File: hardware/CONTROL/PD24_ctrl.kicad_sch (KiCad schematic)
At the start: 7 parts, among them J1 Conn_01x12_Socket, J2 Conn_01x08_Socket, SW1 SW_Push, SW2 SW_Push, SW3 SW_Push, U1 STM32G031G8Ux, U2 ips_0.96_16080

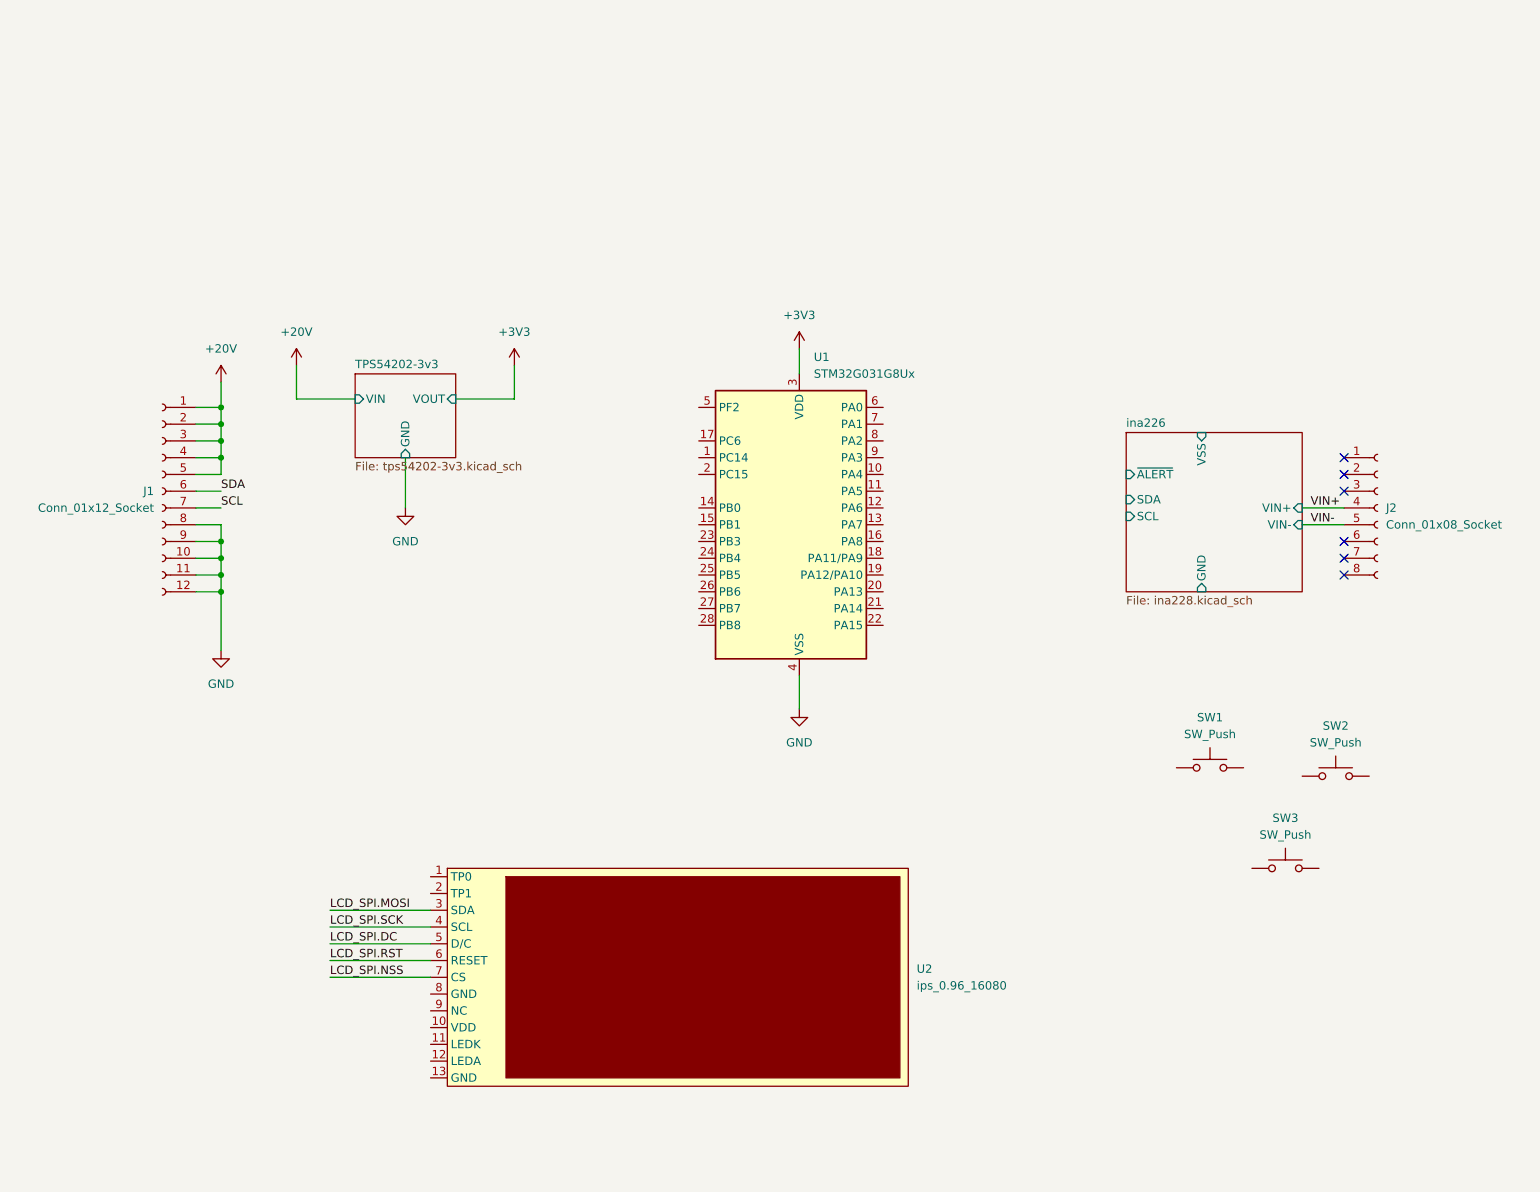
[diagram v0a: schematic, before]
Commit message: PD24 控制部分的PCB设计完成
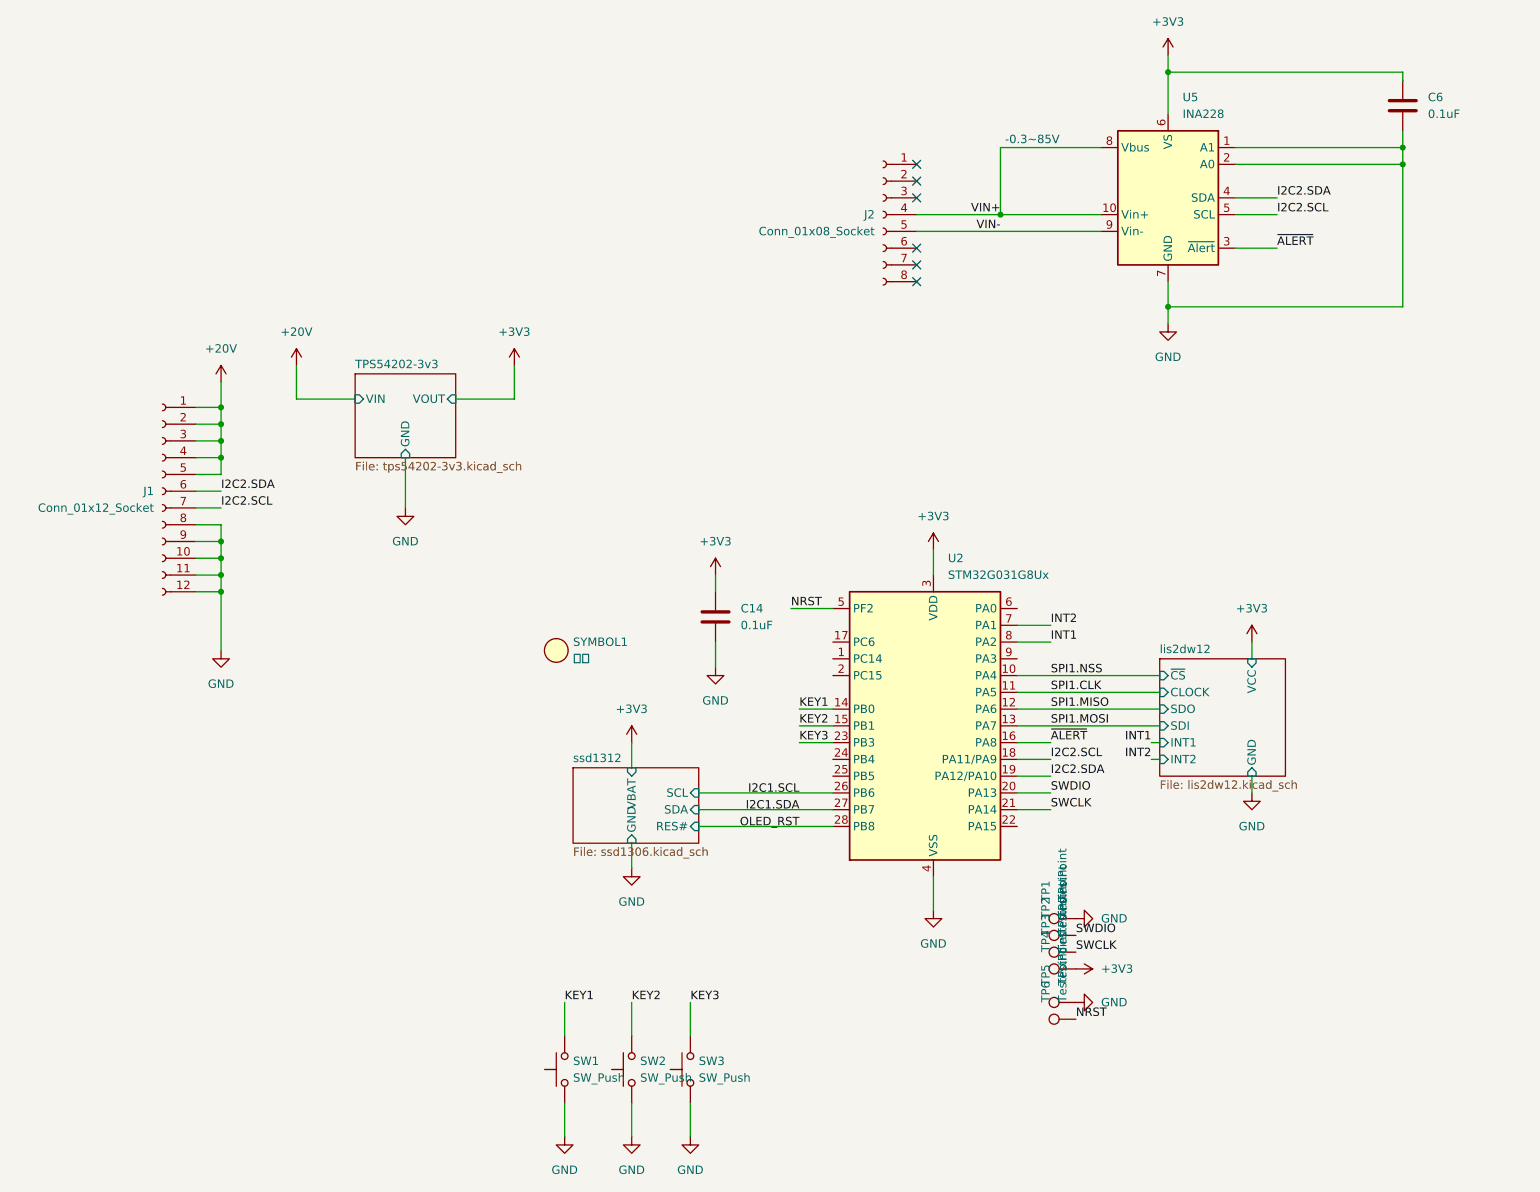
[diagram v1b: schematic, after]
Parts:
- removed U2: ips_0.96_16080, my_footprint:ips-16080-0.96, symbol my_symbol:ips_0.96_16080
- added C14, C6: 0.1uF, Capacitor_SMD:C_0603_1608Metric, symbol Device:C
- added SYMBOL1: 符号, Symbol:KiCad-Logo2_5mm_Copper, symbol my_symbol:symbol
- added TP1, TP2, TP3, TP4, TP5, TP6: TestPoint, TestPoint:TestPoint_Pad_D1.0mm, symbol Connector:TestPoint
- added U5: INA228, Package_SO:VSSOP-10_3x3mm_P0.5mm, symbol Sensor_Energy:INA228
- renumbered U1 to U2
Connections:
- net SCL is gone; now on net I2C2.SCL: J1.7 (Pin_7)
- net SDA is gone; now on net I2C2.SDA: J1.6 (Pin_6)
- net +3V3: now also C14.1, C6.1, TP4.1, U5.6 (VS)
- net GND: now also SW1.1, SW2.1, SW3.1, C14.2, C6.2, TP1.1, TP5.1, U5.1 (A1), U5.2 (A0), U5.7 (GND)
- net VIN+: now also U5.10 (Vin+), U5.8 (Vbus)
- net VIN-: now also U5.9 (Vin-)
- net SPI1.NSS: now reaches U2.10 (PA4)
- net SPI1.CLK: now reaches U2.11 (PA5)
- net SPI1.MISO: now reaches U2.12 (PA6)
- net SPI1.MOSI: now reaches U2.13 (PA7)
- net KEY1: now reaches U2.14 (PB0)
- net KEY1: now also SW1.2
- net KEY2: now reaches U2.15 (PB1)
- net KEY2: now also SW2.2
- net ~{ALERT}: now reaches U2.16 (PA8)
- net ~{ALERT}: now also U5.3 (~{Alert})
- net I2C2.SCL: now reaches U2.18 (PA11/PA9)
- net I2C2.SCL: now also U5.5 (SCL)
- net I2C2.SDA: now reaches U2.19 (PA12/PA10)
- net I2C2.SDA: now also U5.4 (SDA)
- net SWDIO: now reaches U2.20 (PA13)
- net SWDIO: now also TP2.1
- net SWCLK: now reaches U2.21 (PA14)
- net SWCLK: now also TP3.1
- net KEY3: now reaches U2.23 (PB3)
- net KEY3: now also SW3.2
- net ssd1312/SCL: now reaches U2.26 (PB6)
- net ssd1312/SDA: now reaches U2.27 (PB7)
- net ssd1312/RES#: now reaches U2.28 (PB8)
- net NRST: now reaches U2.5 (PF2)
- net NRST: now also TP6.1
- net INT2: now reaches U2.7 (PA1)
- net INT1: now reaches U2.8 (PA2)
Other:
- removed sheet ina226
- added sheet lis2dw12 (lis2dw12.kicad_sch)
- added sheet ssd1312 (ssd1306.kicad_sch)
- note added: "-0.3~85V"
- moved on the sheet: J2, SW1, SW2, SW3, U2

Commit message: 硬件1.0版本更新
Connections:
- net ssd1312/RES# is gone; now on net OLED_RST: U2.28 (PB8)
- net ssd1312/SCL is gone; now on net I2C1.SCL: U2.26 (PB6)
- net ssd1312/SDA is gone; now on net I2C1.SDA: U2.27 (PB7)
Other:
- moved on the sheet: C14, J1, SW1, SW2, SW3, SYMBOL1, TP1, TP2, TP3, TP4, TP5, TP6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

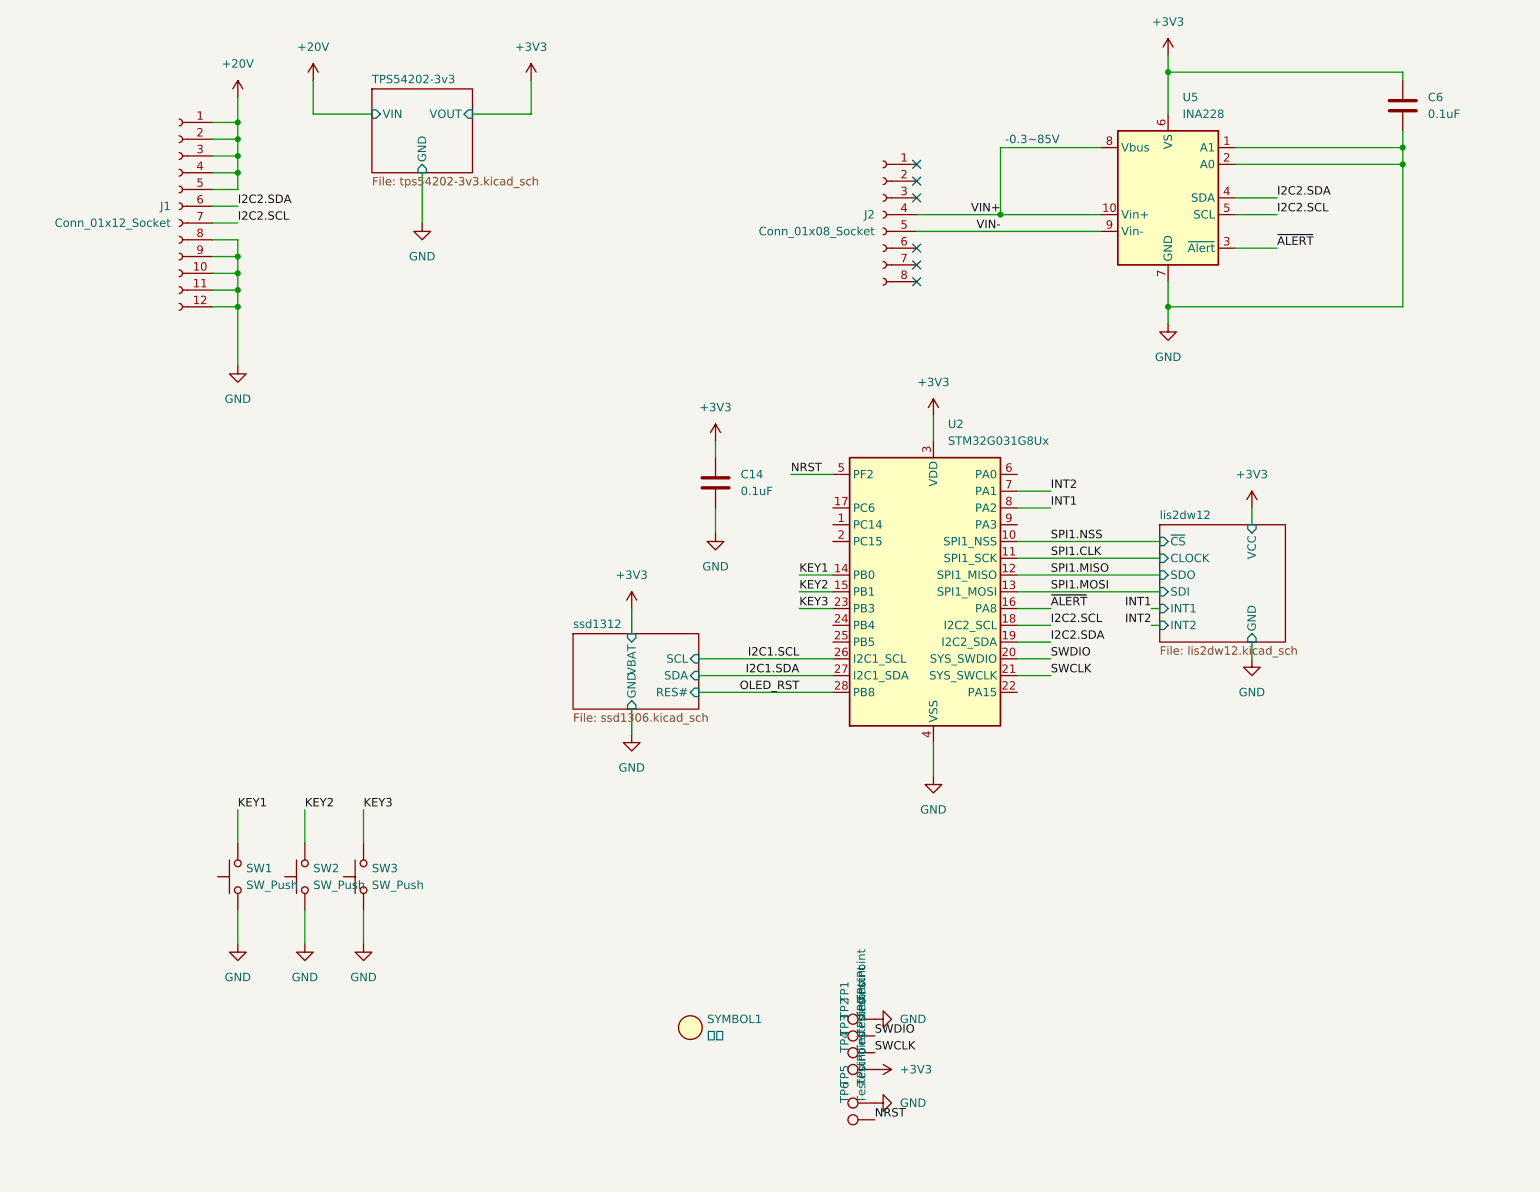
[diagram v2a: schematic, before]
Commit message: 改变了结构，下沉减少厚度
为了实现这个目标，去掉了按键，将原先的buck电路替换成了ldo，但是会产生0.5W的热功耗，acc也放到了电源板上
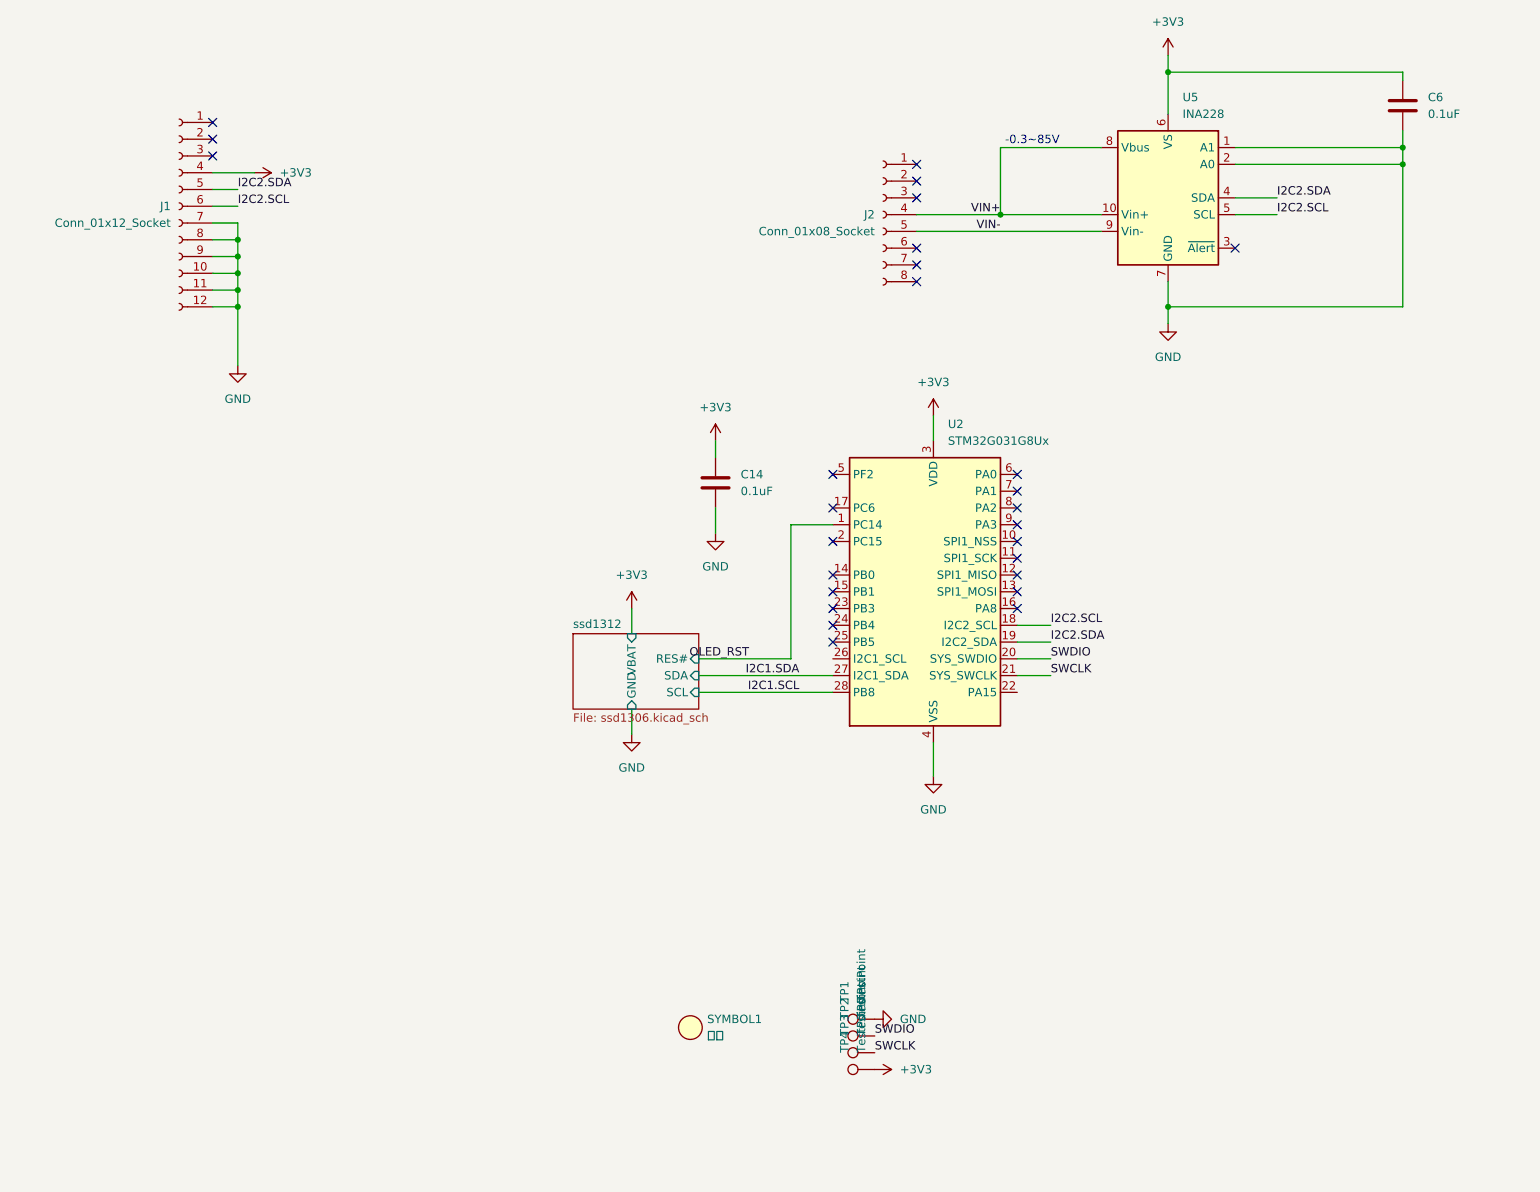
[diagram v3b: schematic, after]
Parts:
- removed SW1, SW2, SW3: SW_Push, my_footprint:KEY-SMD_4P-L4.2-W3.4-P2.15-LS4.5-TL, symbol Switch:SW_Push
- removed TP5, TP6: TestPoint, TestPoint:TestPoint_Pad_D1.0mm, symbol Connector:TestPoint
- C14, C6: footprint Capacitor_SMD:C_0603_1608Metric -> Capacitor_SMD:C_0402_1005Metric
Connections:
- net +3V3: now also J1.4 (Pin_4)
- net GND: now also J1.7 (Pin_7)
- net I2C1.SCL: now also U2.28 (PB8); no longer U2.26 (PB6)
- net I2C2.SCL: now also J1.6 (Pin_6); no longer J1.7 (Pin_7)
- net I2C2.SDA: now also J1.5 (Pin_5); no longer J1.6 (Pin_6)
- net OLED_RST: now also U2.1 (PC14); no longer U2.28 (PB8)
- removed net +20V: J1.1 (Pin_1), J1.2 (Pin_2), J1.3 (Pin_3), J1.4 (Pin_4), J1.5 (Pin_5)
- net INT1: no longer names the net of U2.8 (PA2)
- net INT2: no longer names the net of U2.7 (PA1)
- net KEY1: no longer names the net of U2.14 (PB0)
- net KEY2: no longer names the net of U2.15 (PB1)
- net KEY3: no longer names the net of U2.23 (PB3)
- net NRST: no longer names the net of U2.5 (PF2)
- net SPI1.CLK: no longer names the net of U2.11 (PA5)
- net SPI1.MISO: no longer names the net of U2.12 (PA6)
- net SPI1.MOSI: no longer names the net of U2.13 (PA7)
- net SPI1.NSS: no longer names the net of U2.10 (PA4)
- net ~{ALERT}: no longer names the net of U2.16 (PA8)
- net ~{ALERT}: no longer U5.3 (~{Alert})
- no-connect marks 6 -> 27
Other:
- removed sheet TPS54202-3v3
- removed sheet lis2dw12

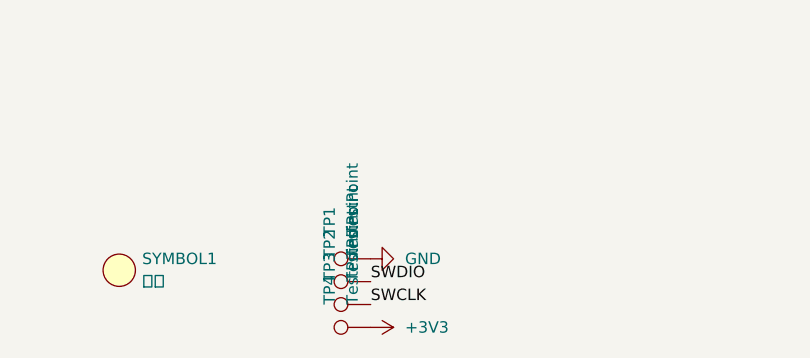
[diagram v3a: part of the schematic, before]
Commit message: 优化了布局的结构，使其能够在缩小的板框能够单面布局，适合焊接且不影响屏幕贴装
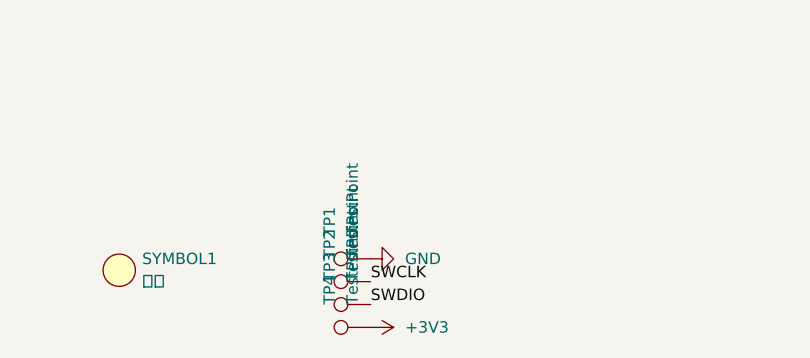
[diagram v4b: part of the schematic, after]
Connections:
- net SWCLK: now also TP2.1; no longer TP3.1
- net SWDIO: now also TP3.1; no longer TP2.1
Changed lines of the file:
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@@
-		)
-	)
-	(label "SWCLK"
-		(at 135.89 176.53 0)
-		(fields_autoplaced yes)
-		(effects
-			(font
-				(size 1.27 1.27)
-			)
-			(justify left bottom)
 		)
 	)
@@
 		)
 	)
-	(label "SWDIO"
+	(label "SWCLK"
 		(at 135.89 173.99 0)
 		(fields_autoplaced yes)
 		(effects
+			(font
+				(size 1.27 1.27)
+			)
+			(justify left bottom)
+		)
+	)
+	(label "SWDIO"
+		(at 135.89 176.53 0)
+		(fields_autoplaced yes)
+		(effects
